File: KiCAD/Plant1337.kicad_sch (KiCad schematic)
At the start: 43 parts, among them Q1 AO3400A, Q2 AO3400A, Q3 AO3400A, Q4 AO3400A, U1 SHTC3

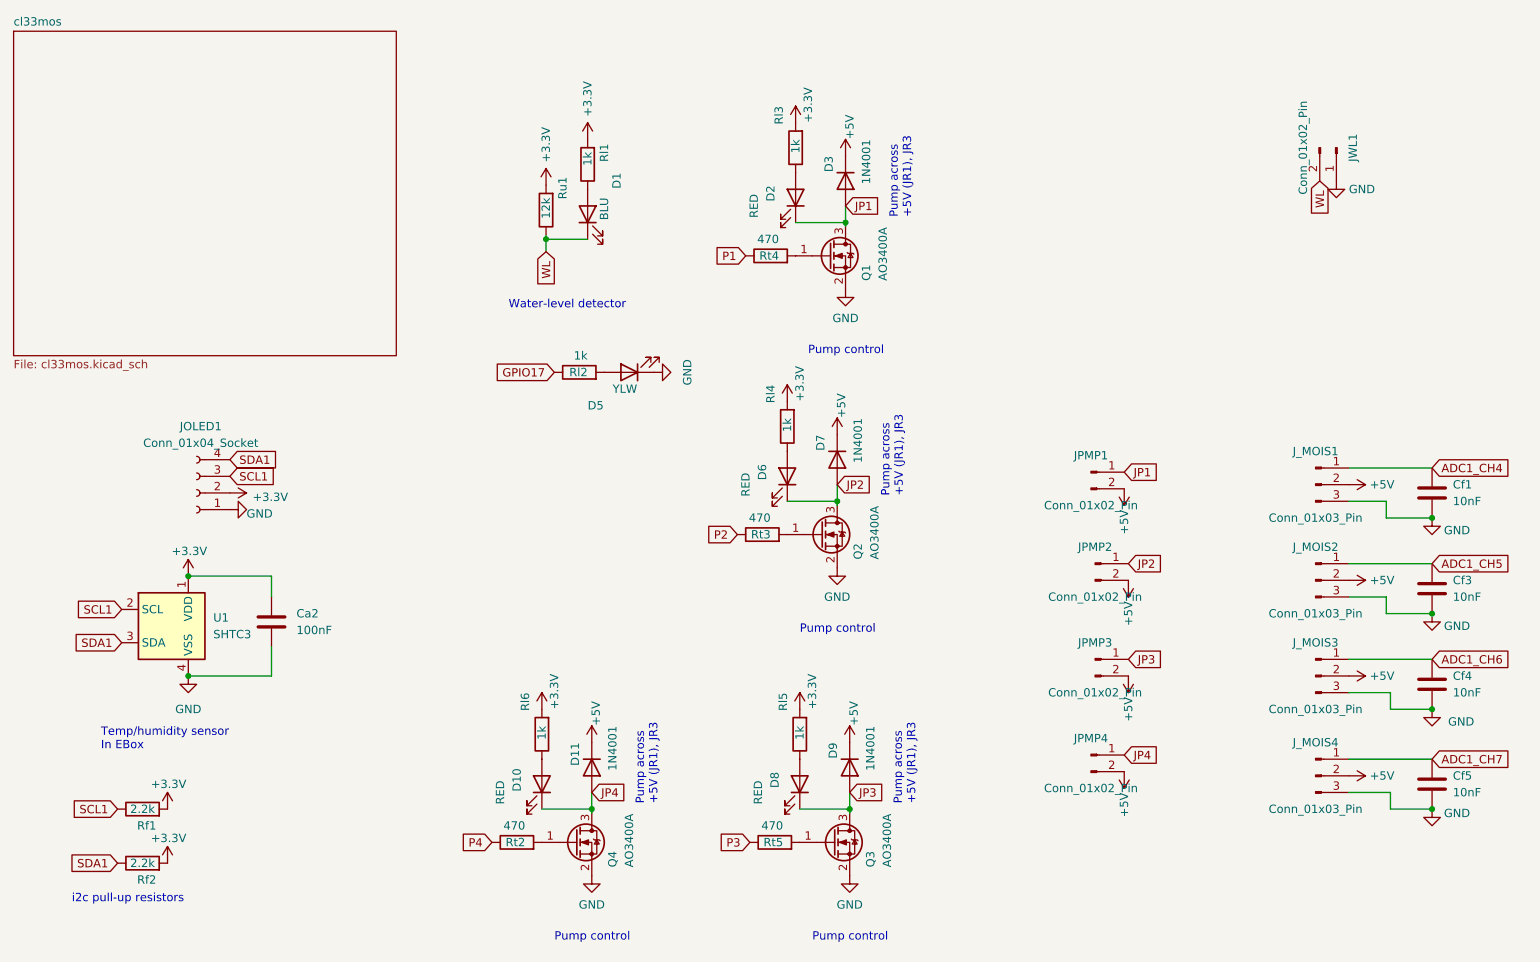
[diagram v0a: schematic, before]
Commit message: Support for board 2.0: USB-C, ESP32-C3-WROOM1-B8R2
Need to make new board version a new compiler def and ifdef new pin assignments.
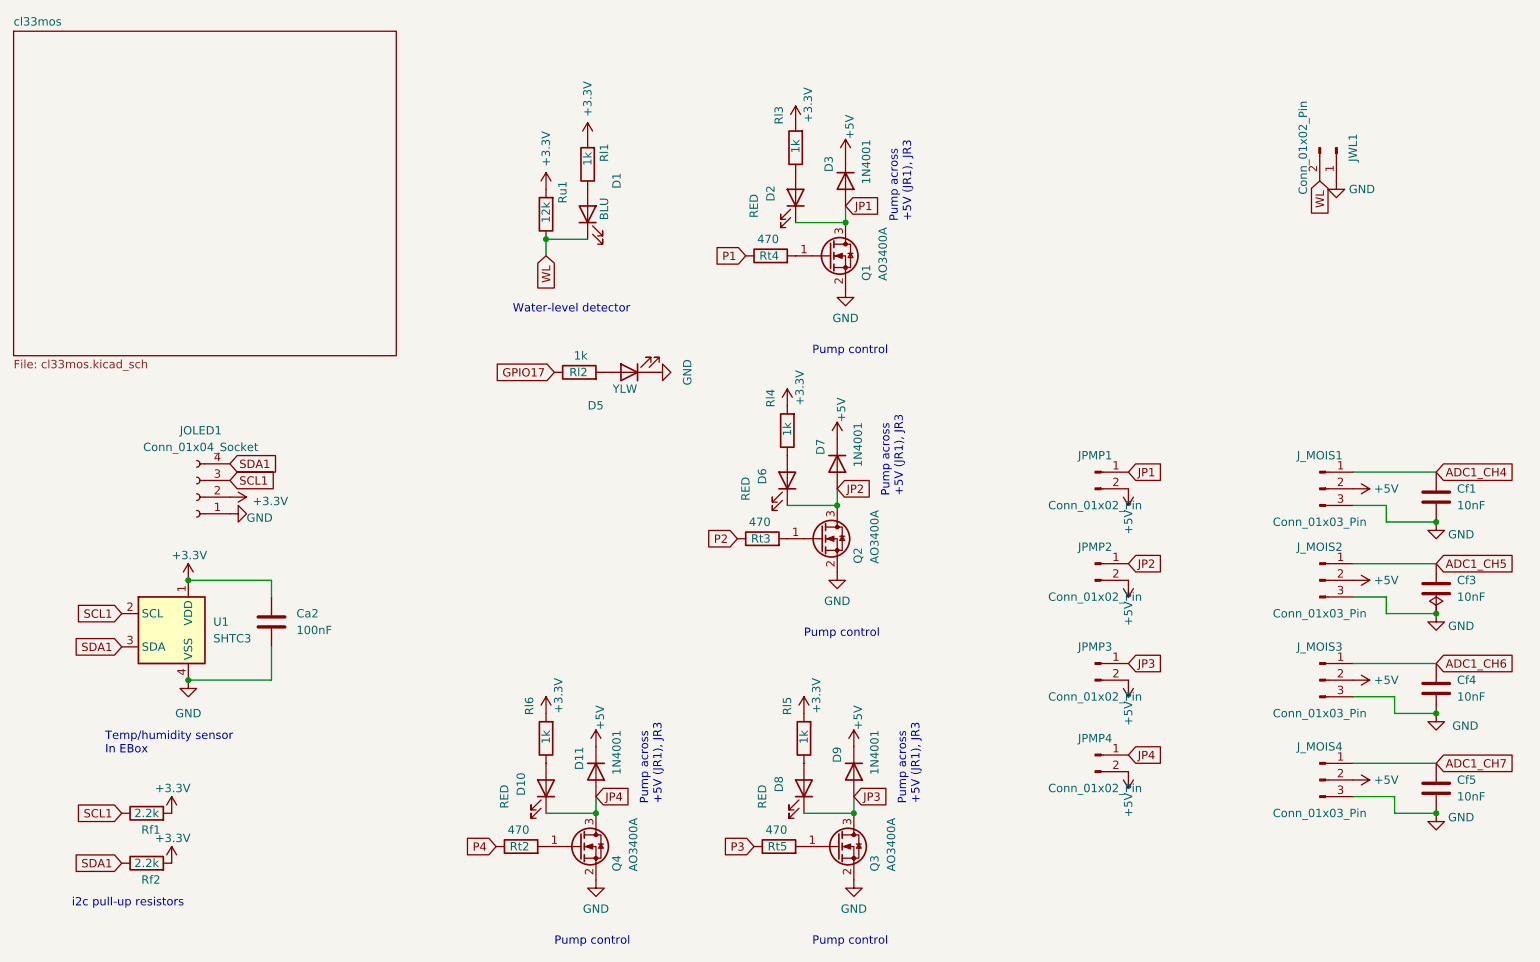
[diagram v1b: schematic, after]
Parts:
- D11, D3, D7, D9: footprint Diode_SMD:D_SMA -> chl33_library:DO-216
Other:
- moved on the sheet: Cf1, Cf3, Cf4, Cf5, D10, D11, D6, D7, D8, D9, JOLED1, JPMP1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

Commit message: Update PCB layout/schematic: fix flybck diodes
Had wrong footprint
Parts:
- D11, D3, D7, D9: footprint chl33_library:DO-216 -> Diode_SMD:D_SMA
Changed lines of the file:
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@@
 			)
 		)
-		(property "Footprint" "chl33_library:DO-216"
+		(property "Footprint" "Diode_SMD:D_SMA"
 			(at 141.605 133.35 0)
 			(effects
@@
 			)
 		)
-		(property "Footprint" "chl33_library:DO-216"
+		(property "Footprint" "Diode_SMD:D_SMA"
 			(at 140.335 43.18 0)
 			(effects
@@
 			)
 		)
-		(property "Footprint" "chl33_library:DO-216"
+		(property "Footprint" "Diode_SMD:D_SMA"
 			(at 102.235 133.35 0)
 			(effects
@@
 			)
 		)
-		(property "Footprint" "chl33_library:DO-216"
+		(property "Footprint" "Diode_SMD:D_SMA"
 			(at 139.065 86.36 0)
 			(effects
